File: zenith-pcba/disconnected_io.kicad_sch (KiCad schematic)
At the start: 1 part, among them U1 XC7K70T-FBG676

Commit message: chore(pcba): clean up pages
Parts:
- removed U1: XC7K70T-FBG676, easyeda2kicad:FBGA-676_L27.0-W27.0-R26-C26-P1.00-BL, symbol FPGA_Xilinx_Kintex7:XC7K70T-FBG676
- added U1: XC7K70T-FBG676, easyeda2kicad:FBGA-676_L27.0-W27.0-R26-C26-P1.00-BL, symbol FPGA_Xilinx_Kintex7:XC7K70T-FBG676

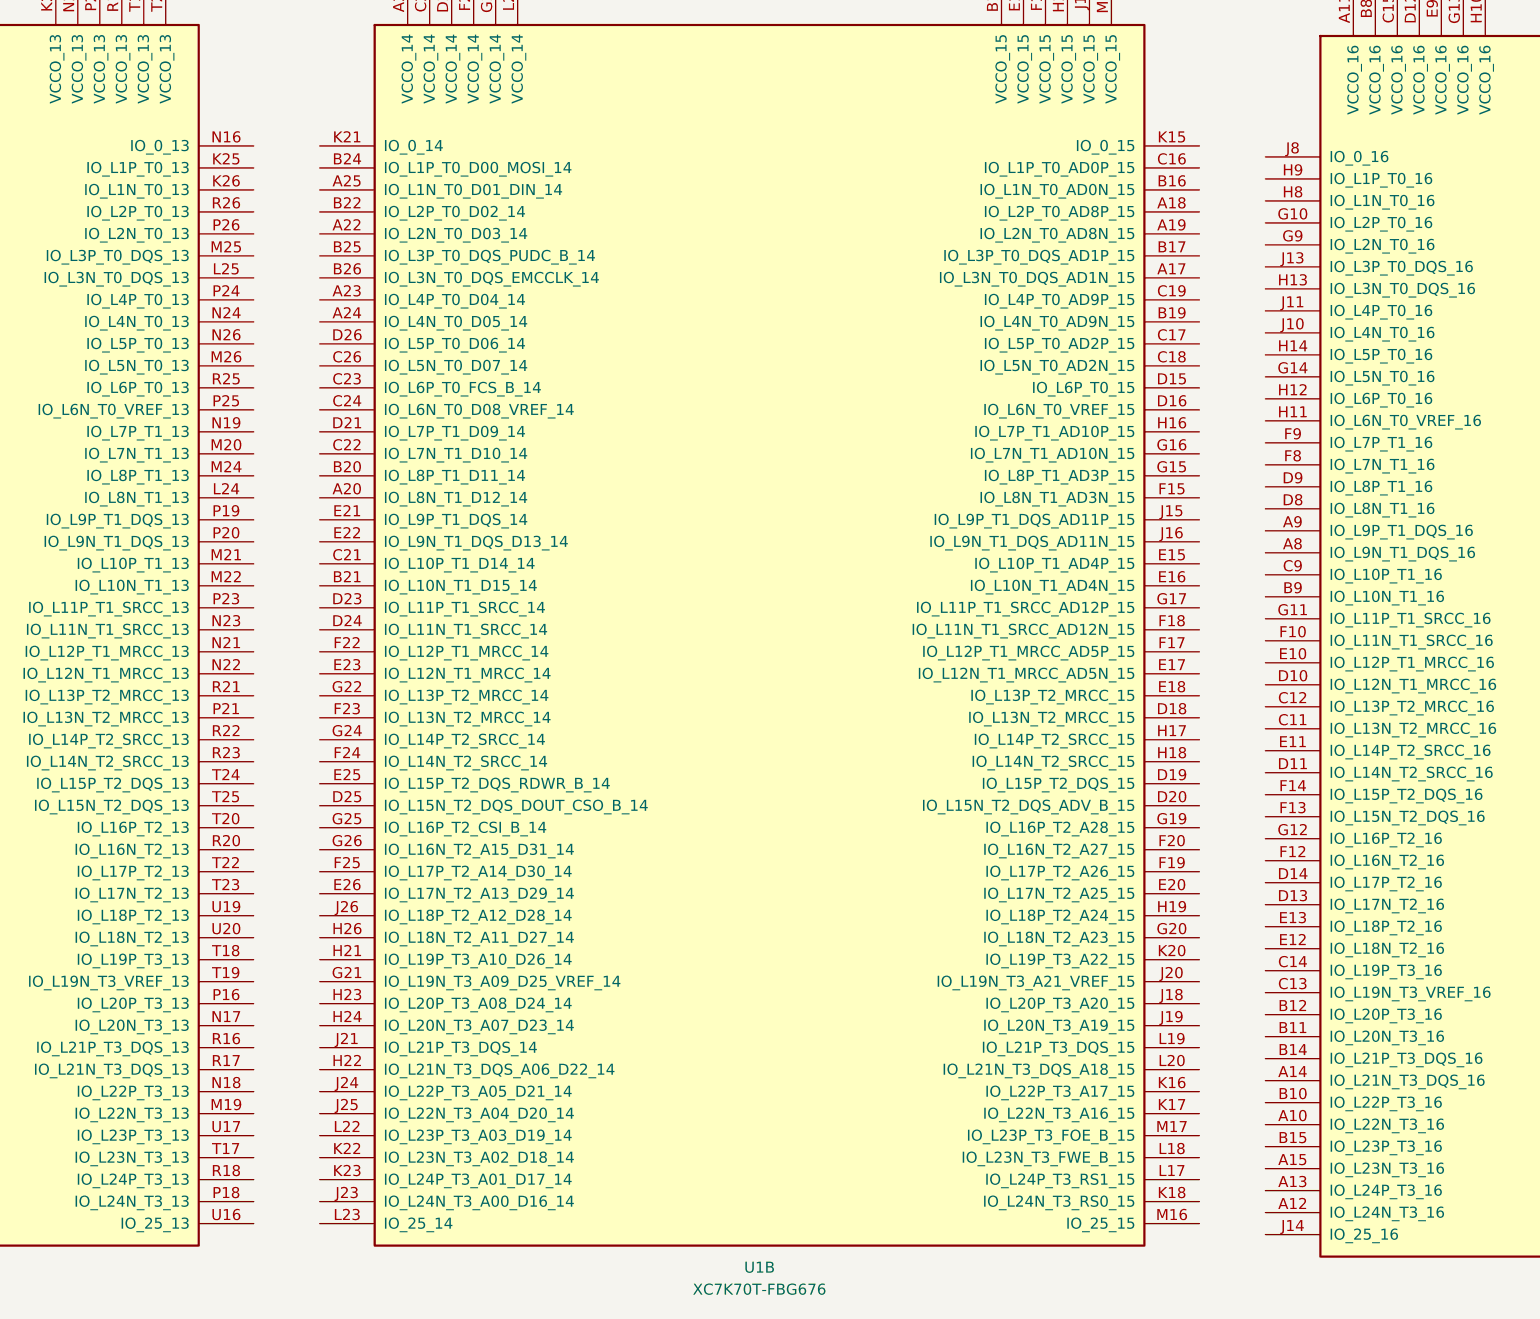
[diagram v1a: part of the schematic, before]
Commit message: feat(hardware): ddr3 sodimm import
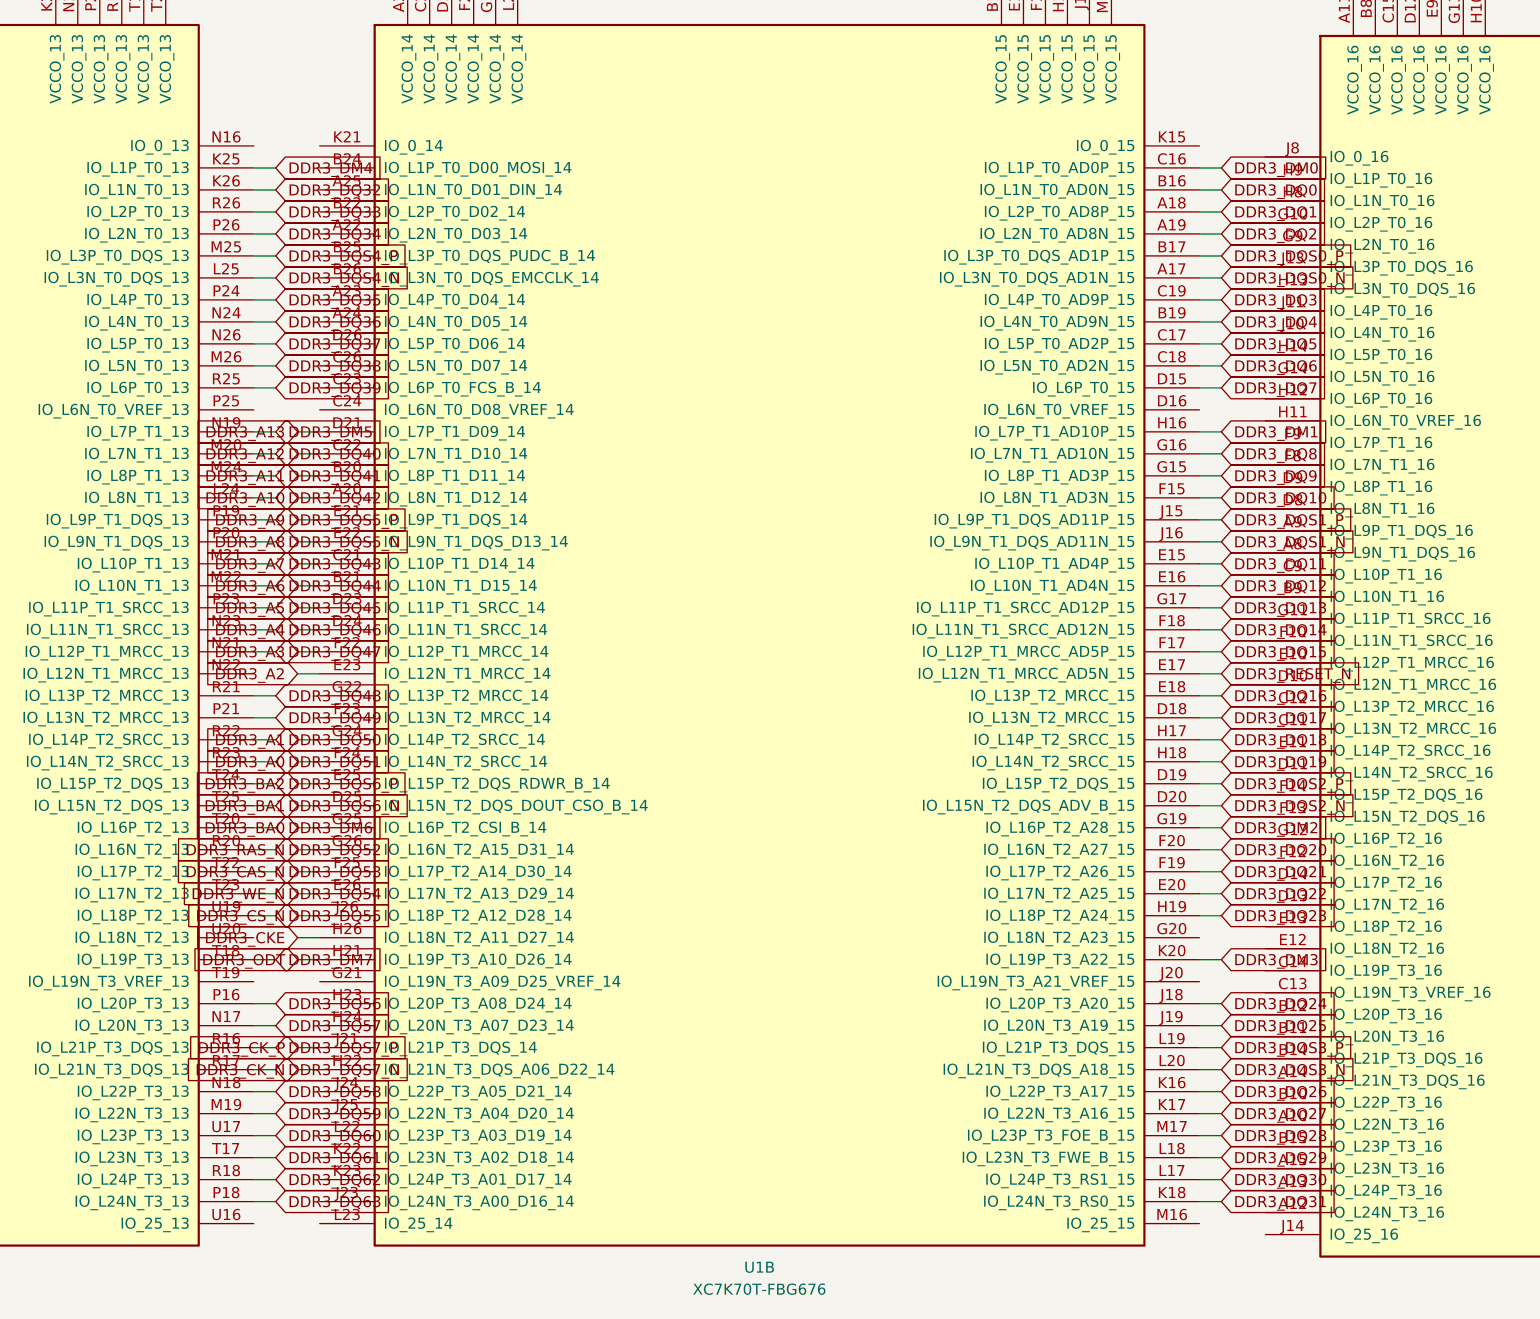
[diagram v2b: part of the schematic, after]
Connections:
- net DDR3_DM4: now reaches U1.K25 (IO_L1P_T0_13)
- net DDR3_DQ32: now reaches U1.K26 (IO_L1N_T0_13)
- net DDR3_DQ42: now reaches U1.L24 (IO_L8N_T1_13)
- net DDR3_DQS4_N: now reaches U1.L25 (IO_L3N_T0_DQS_13)
- net DDR3_DQ59: now reaches U1.M19 (IO_L22N_T3_13)
- net DDR3_DQ40: now reaches U1.M20 (IO_L7N_T1_13)
- net DDR3_DQ43: now reaches U1.M21 (IO_L10P_T1_13)
- net DDR3_DQ44: now reaches U1.M22 (IO_L10N_T1_13)
- net DDR3_DQ41: now reaches U1.M24 (IO_L8P_T1_13)
- net DDR3_DQS4_P: now reaches U1.M25 (IO_L3P_T0_DQS_13)
- net DDR3_DQ38: now reaches U1.M26 (IO_L5N_T0_13)
- net DDR3_DQ57: now reaches U1.N17 (IO_L20N_T3_13)
- net DDR3_DQ58: now reaches U1.N18 (IO_L22P_T3_13)
- net DDR3_DM5: now reaches U1.N19 (IO_L7P_T1_13)
- net DDR3_DQ47: now reaches U1.N21 (IO_L12P_T1_MRCC_13)
- net DDR3_DQ46: now reaches U1.N23 (IO_L11N_T1_SRCC_13)
- net DDR3_DQ36: now reaches U1.N24 (IO_L4N_T0_13)
- net DDR3_DQ37: now reaches U1.N26 (IO_L5P_T0_13)
- net DDR3_DQ56: now reaches U1.P16 (IO_L20P_T3_13)
- net DDR3_DQ63: now reaches U1.P18 (IO_L24N_T3_13)
- net DDR3_DQS5_P: now reaches U1.P19 (IO_L9P_T1_DQS_13)
- net DDR3_DQS5_N: now reaches U1.P20 (IO_L9N_T1_DQS_13)
- net DDR3_DQ49: now reaches U1.P21 (IO_L13N_T2_MRCC_13)
- net DDR3_DQ45: now reaches U1.P23 (IO_L11P_T1_SRCC_13)
- net DDR3_DQ35: now reaches U1.P24 (IO_L4P_T0_13)
- net DDR3_DQ34: now reaches U1.P26 (IO_L2N_T0_13)
- net DDR3_DQS7_P: now reaches U1.R16 (IO_L21P_T3_DQS_13)
- net DDR3_DQS7_N: now reaches U1.R17 (IO_L21N_T3_DQS_13)
- net DDR3_DQ62: now reaches U1.R18 (IO_L24P_T3_13)
- net DDR3_DQ52: now reaches U1.R20 (IO_L16N_T2_13)
- net DDR3_DQ48: now reaches U1.R21 (IO_L13P_T2_MRCC_13)
- net DDR3_DQ50: now reaches U1.R22 (IO_L14P_T2_SRCC_13)
- net DDR3_DQ51: now reaches U1.R23 (IO_L14N_T2_SRCC_13)
- net DDR3_DQ39: now reaches U1.R25 (IO_L6P_T0_13)
- net DDR3_DQ33: now reaches U1.R26 (IO_L2P_T0_13)
- net DDR3_DQ61: now reaches U1.T17 (IO_L23N_T3_13)
- net DDR3_DM7: now reaches U1.T18 (IO_L19P_T3_13)
- net DDR3_DM6: now reaches U1.T20 (IO_L16P_T2_13)
- net DDR3_DQ53: now reaches U1.T22 (IO_L17P_T2_13)
- net DDR3_DQ54: now reaches U1.T23 (IO_L17N_T2_13)
- net DDR3_DQS6_P: now reaches U1.T24 (IO_L15P_T2_DQS_13)
- net DDR3_DQS6_N: now reaches U1.T25 (IO_L15N_T2_DQS_13)
- net DDR3_DQ60: now reaches U1.U17 (IO_L23P_T3_13)
- net DDR3_DQ55: now reaches U1.U19 (IO_L18P_T2_13)
- net DDR3_DQS0_N: now reaches U1.A17 (IO_L3N_T0_DQS_AD1N_15)
- net DDR3_DQ1: now reaches U1.A18 (IO_L2P_T0_AD8P_15)
- net DDR3_DQ2: now reaches U1.A19 (IO_L2N_T0_AD8N_15)
- net DDR3_A10: now reaches U1.A20 (IO_L8N_T1_D12_14)
- net DDR3_DQ0: now reaches U1.B16 (IO_L1N_T0_AD0N_15)
- net DDR3_DQS0_P: now reaches U1.B17 (IO_L3P_T0_DQS_AD1P_15)
- net DDR3_DQ4: now reaches U1.B19 (IO_L4N_T0_AD9N_15)
- net DDR3_A11: now reaches U1.B20 (IO_L8P_T1_D11_14)
- net DDR3_A6: now reaches U1.B21 (IO_L10N_T1_D15_14)
- net DDR3_DM0: now reaches U1.C16 (IO_L1P_T0_AD0P_15)
- net DDR3_DQ5: now reaches U1.C17 (IO_L5P_T0_AD2P_15)
- net DDR3_DQ6: now reaches U1.C18 (IO_L5N_T0_AD2N_15)
- net DDR3_DQ3: now reaches U1.C19 (IO_L4P_T0_AD9P_15)
- net DDR3_A7: now reaches U1.C21 (IO_L10P_T1_D14_14)
- net DDR3_A12: now reaches U1.C22 (IO_L7N_T1_D10_14)
- net DDR3_DQ7: now reaches U1.D15 (IO_L6P_T0_15)
- net DDR3_DQ17: now reaches U1.D18 (IO_L13N_T2_MRCC_15)
- net DDR3_DQS2_P: now reaches U1.D19 (IO_L15P_T2_DQS_15)
- net DDR3_DQS2_N: now reaches U1.D20 (IO_L15N_T2_DQS_ADV_B_15)
- net DDR3_A13: now reaches U1.D21 (IO_L7P_T1_D09_14)
- net DDR3_A5: now reaches U1.D23 (IO_L11P_T1_SRCC_14)
- net DDR3_A4: now reaches U1.D24 (IO_L11N_T1_SRCC_14)
- net DDR3_BA1: now reaches U1.D25 (IO_L15N_T2_DQS_DOUT_CSO_B_14)
- net DDR3_DQ11: now reaches U1.E15 (IO_L10P_T1_AD4P_15)
- net DDR3_DQ12: now reaches U1.E16 (IO_L10N_T1_AD4N_15)
- net DDR3_RESET_N: now reaches U1.E17 (IO_L12N_T1_MRCC_AD5N_15)
- net DDR3_DQ16: now reaches U1.E18 (IO_L13P_T2_MRCC_15)
- net DDR3_DQ22: now reaches U1.E20 (IO_L17N_T2_A25_15)
- net DDR3_A9: now reaches U1.E21 (IO_L9P_T1_DQS_14)
- net DDR3_A8: now reaches U1.E22 (IO_L9N_T1_DQS_D13_14)
- net DDR3_A2: now reaches U1.E23 (IO_L12N_T1_MRCC_14)
- net DDR3_BA2: now reaches U1.E25 (IO_L15P_T2_DQS_RDWR_B_14)
- net DDR3_WE_N: now reaches U1.E26 (IO_L17N_T2_A13_D29_14)
- net DDR3_DQ10: now reaches U1.F15 (IO_L8N_T1_AD3N_15)
- net DDR3_DQ15: now reaches U1.F17 (IO_L12P_T1_MRCC_AD5P_15)
- net DDR3_DQ14: now reaches U1.F18 (IO_L11N_T1_SRCC_AD12N_15)
- net DDR3_DQ21: now reaches U1.F19 (IO_L17P_T2_A26_15)
- net DDR3_DQ20: now reaches U1.F20 (IO_L16N_T2_A27_15)
- net DDR3_A3: now reaches U1.F22 (IO_L12P_T1_MRCC_14)
- net DDR3_A0: now reaches U1.F24 (IO_L14N_T2_SRCC_14)
- net DDR3_CAS_N: now reaches U1.F25 (IO_L17P_T2_A14_D30_14)
- net DDR3_DQ9: now reaches U1.G15 (IO_L8P_T1_AD3P_15)
- net DDR3_DQ8: now reaches U1.G16 (IO_L7N_T1_AD10N_15)
- net DDR3_DQ13: now reaches U1.G17 (IO_L11P_T1_SRCC_AD12P_15)
- net DDR3_DM2: now reaches U1.G19 (IO_L16P_T2_A28_15)
- net DDR3_A1: now reaches U1.G24 (IO_L14P_T2_SRCC_14)
- net DDR3_BA0: now reaches U1.G25 (IO_L16P_T2_CSI_B_14)
- net DDR3_RAS_N: now reaches U1.G26 (IO_L16N_T2_A15_D31_14)
- net DDR3_DM1: now reaches U1.H16 (IO_L7P_T1_AD10P_15)
- net DDR3_DQ18: now reaches U1.H17 (IO_L14P_T2_SRCC_15)
- net DDR3_DQ19: now reaches U1.H18 (IO_L14N_T2_SRCC_15)
- net DDR3_DQ23: now reaches U1.H19 (IO_L18P_T2_A24_15)
- net DDR3_ODT: now reaches U1.H21 (IO_L19P_T3_A10_D26_14)
- net DDR3_CK_N: now reaches U1.H22 (IO_L21N_T3_DQS_A06_D22_14)
- net DDR3_CKE: now reaches U1.H26 (IO_L18N_T2_A11_D27_14)
- net DDR3_DQS1_P: now reaches U1.J15 (IO_L9P_T1_DQS_AD11P_15)
- net DDR3_DQS1_N: now reaches U1.J16 (IO_L9N_T1_DQS_AD11N_15)
- net DDR3_DQ24: now reaches U1.J18 (IO_L20P_T3_A20_15)
- net DDR3_DQ25: now reaches U1.J19 (IO_L20N_T3_A19_15)
- net DDR3_CK_P: now reaches U1.J21 (IO_L21P_T3_DQS_14)
- net DDR3_CS_N: now reaches U1.J26 (IO_L18P_T2_A12_D28_14)
- net DDR3_DQ26: now reaches U1.K16 (IO_L22P_T3_A17_15)
- net DDR3_DQ27: now reaches U1.K17 (IO_L22N_T3_A16_15)
- net DDR3_DQ31: now reaches U1.K18 (IO_L24N_T3_RS0_15)
- net DDR3_DM3: now reaches U1.K20 (IO_L19P_T3_A22_15)
- net DDR3_DQ30: now reaches U1.L17 (IO_L24P_T3_RS1_15)
- net DDR3_DQ29: now reaches U1.L18 (IO_L23N_T3_FWE_B_15)
- net DDR3_DQS3_P: now reaches U1.L19 (IO_L21P_T3_DQS_15)
- net DDR3_DQS3_N: now reaches U1.L20 (IO_L21N_T3_DQS_A18_15)
- net DDR3_DQ28: now reaches U1.M17 (IO_L23P_T3_FOE_B_15)
